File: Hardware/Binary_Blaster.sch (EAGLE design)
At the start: 26 parts

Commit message: cleaned up part values on buttons
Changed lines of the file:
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@@
 <part name="P+9" library="SparkFun" deviceset="3.3V" device=""/>
 <part name="GND1" library="SparkFun" deviceset="GND" device=""/>
-<part name="S3" library="SparkFun-Electromechanical" deviceset="SWITCH-MOMENTARY-LED" device="EZ" value="SWITCH-MOMENTARY-LEDEZ"/>
-<part name="S4" library="SparkFun-Electromechanical" deviceset="SWITCH-MOMENTARY-LED" device="EZ" value="SWITCH-MOMENTARY-LEDEZ"/>
-<part name="S5" library="SparkFun-Electromechanical" deviceset="SWITCH-MOMENTARY-LED" device="EZ" value="SWITCH-MOMENTARY-LEDEZ"/>
-<part name="S6" library="SparkFun-Electromechanical" deviceset="SWITCH-MOMENTARY-LED" device="EZ" value="SWITCH-MOMENTARY-LEDEZ"/>
+<part name="S3" library="SparkFun-Electromechanical" deviceset="SWITCH-MOMENTARY-LED" device="EZ" value=""/>
+<part name="S4" library="SparkFun-Electromechanical" deviceset="SWITCH-MOMENTARY-LED" device="EZ" value=""/>
+<part name="S5" library="SparkFun-Electromechanical" deviceset="SWITCH-MOMENTARY-LED" device="EZ" value=""/>
+<part name="S6" library="SparkFun-Electromechanical" deviceset="SWITCH-MOMENTARY-LED" device="EZ" value=""/>
 <part name="GND3" library="SparkFun" deviceset="GND" device=""/>
 <part name="LOGO1" library="SparkFun-Aesthetics" deviceset="LOGO-SFE" device="NEW" value="LOGO-SFENEW"/>

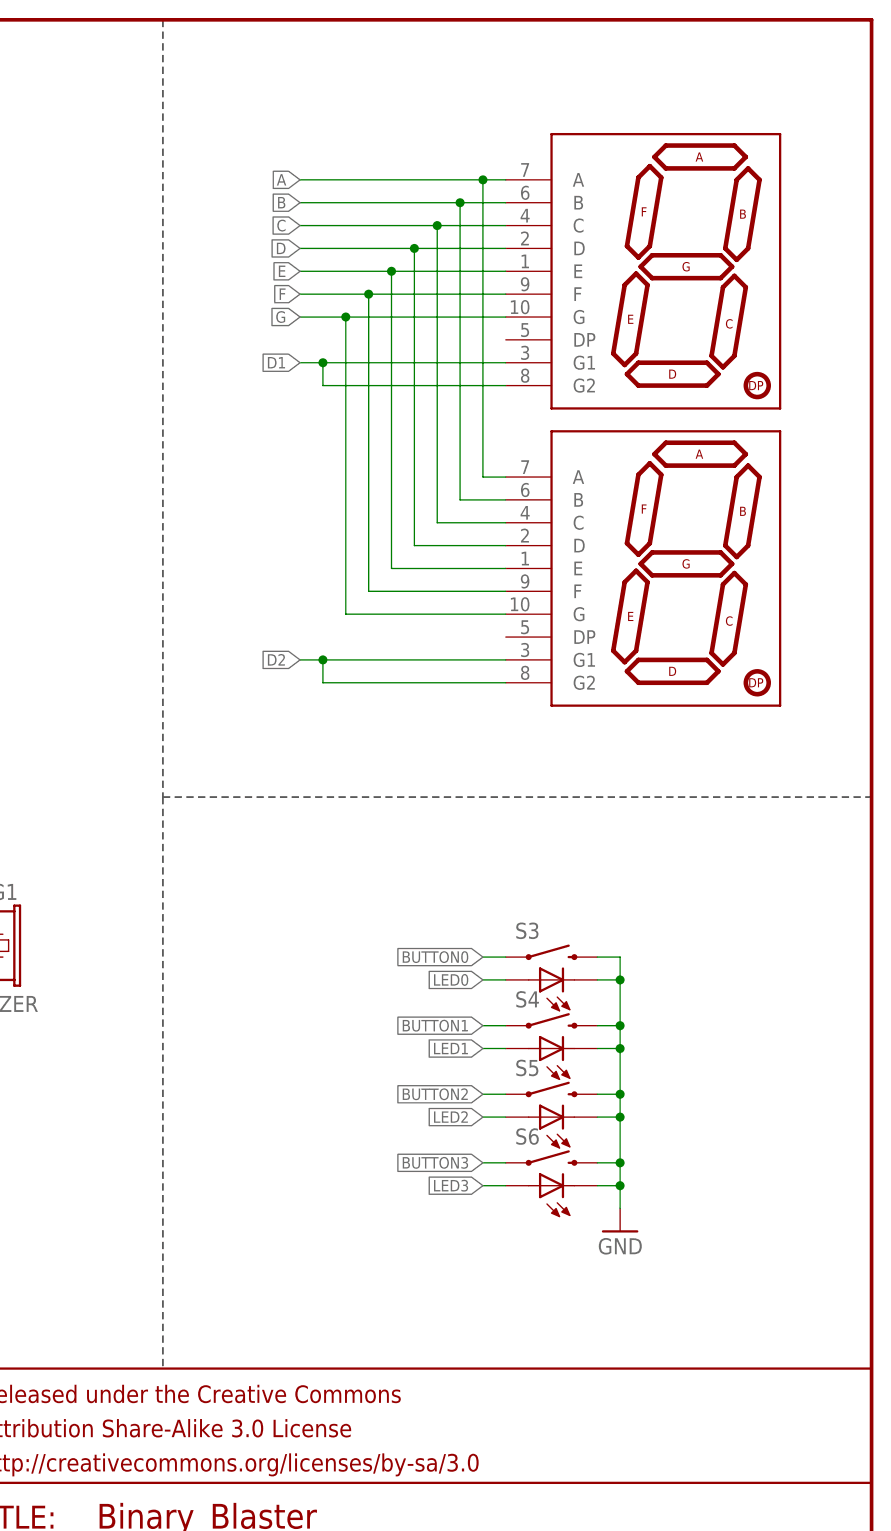
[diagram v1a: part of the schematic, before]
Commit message: Added LED polarity swap trick
Still V03
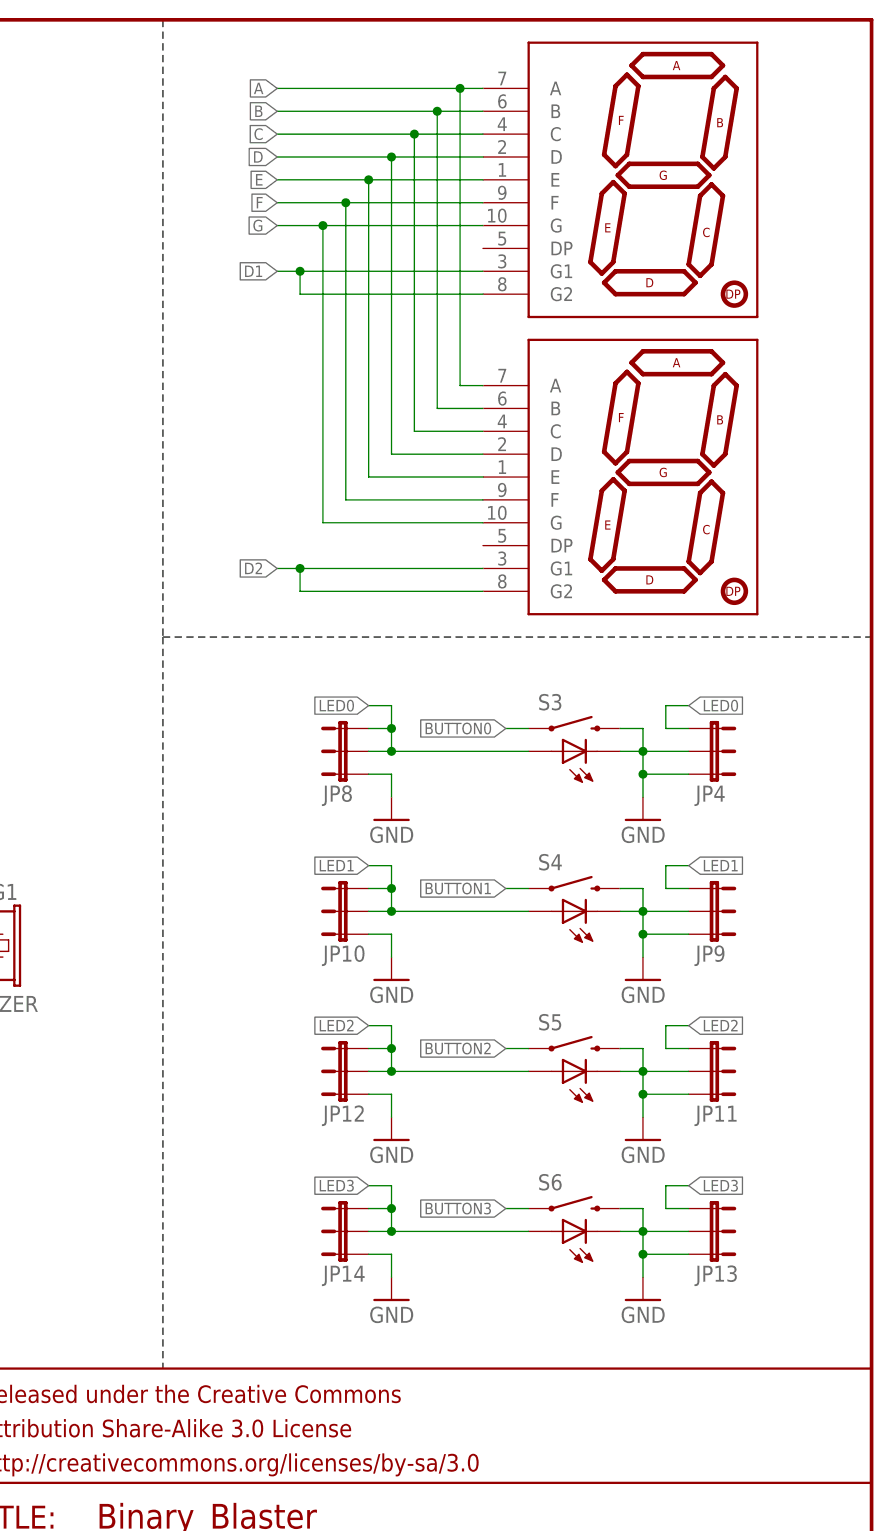
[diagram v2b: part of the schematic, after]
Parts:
- added JP10, JP11, JP12, JP13, JP14, JP4, JP8, JP9: JUMPER-3SMD, SparkFun-Passives:JUMPER-3SMD
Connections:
- net GND: now also JP10.1, JP11.2, JP11.3, JP12.1, JP13.2, JP13.3, JP14.1, JP4.2, JP4.3, JP8.1, JP9.2, JP9.3
- net LED0: now also JP4.1, JP8.2, JP8.3
- net LED1: now also JP10.2, JP10.3, JP9.1
- net LED2: now also JP11.1, JP12.2, JP12.3
- net LED3: now also JP13.1, JP14.2, JP14.3
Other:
- moved on the sheet: S3, S4, S5, S6

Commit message: V10
-changed bottom copper version to "v10"
-added "pete lewis" to designed by on board tname layer
-changed version to "10" on schematic
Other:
- note added: "10"
- note removed: "1"
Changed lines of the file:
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@@
 <sheet>
 <plain>
-<text x="243.84" y="7.62" size="2.54" layer="94">1</text>
+<text x="243.84" y="7.62" size="2.54" layer="94">10</text>
 <text x="157.48" y="7.62" size="1.778" layer="94">Pete Lewis</text>
 <wire x1="170.18" y1="185.42" x2="170.18" y2="116.84" width="0.2032" layer="97" style="shortdash"/>
